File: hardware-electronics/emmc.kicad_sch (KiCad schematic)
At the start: 42 parts, among them J7 TC2030-IDC-NL, U2 EMMC16G-MW28-01E10, U4 24AA04T-I_OT, U8 USB2244-AEZG-06, Y2 ECS-240-10-47-CKM-TR

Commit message: [#26] Correct MPN GRM155R61H105KE05D
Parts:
- C11, C12, C14, C21, C7, C9: Author Your Name -> Lukasz Nowarkiewicz; MPN GRM155R61H105KE92D -> GRM155R61H105KE05D
- C17: Author Your Name -> Lukasz Nowarkiewicz; MPN GRM155R61H105KE92D -> GRM155R61H105KE05D; now left out of the parts list
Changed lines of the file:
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@@
 			)
 		)
-		(property "MPN" "GRM155R61H105KE92D"
+		(property "MPN" "GRM155R61H105KE05D"
 			(at 237.49 83.82 0)
 			(effects
@@
 			)
 		)
-		(property "Author" "Your Name"
+		(property "Author" "Lukasz Nowarkiewicz"
 			(at 245.11 83.82 0)
 			(effects
@@
 		(unit 1)
 		(exclude_from_sim no)
-		(in_bom yes)
+		(in_bom no)
 		(on_board yes)
 		(dnp no)
@@
 			)
 		)
-		(property "MPN" "GRM155R61H105KE92D"
+		(property "MPN" "GRM155R61H105KE05D"
 			(at 220.98 91.44 0)
 			(effects
@@
 			)
 		)
-		(property "Author" "Your Name"
+		(property "Author" "Lukasz Nowarkiewicz"
 			(at 228.6 91.44 0)
 			(effects
@@
 			)
 		)
-		(property "MPN" "GRM155R61H105KE92D"
+		(property "MPN" "GRM155R61H105KE05D"
 			(at 278.13 80.01 0)
 			(effects
@@
 			)
 		)
-		(property "Author" "Your Name"
+		(property "Author" "Lukasz Nowarkiewicz"
 			(at 285.75 80.01 0)
 			(effects
@@
 			)
 		)
-		(property "MPN" "GRM155R61H105KE92D"
+		(property "MPN" "GRM155R61H105KE05D"
 			(at 34.29 66.04 0)
 			(effects
@@
 			)
 		)
-		(property "Author" "Your Name"
+		(property "Author" "Lukasz Nowarkiewicz"
 			(at 41.91 66.04 0)
 			(effects
@@
 			)
 		)
-		(property "MPN" "GRM155R61H105KE92D"
+		(property "MPN" "GRM155R61H105KE05D"
 			(at 255.27 83.82 0)
 			(effects
@@
 			)
 		)
-		(property "Author" "Your Name"
+		(property "Author" "Lukasz Nowarkiewicz"
 			(at 262.89 83.82 0)
 			(effects
@@
 			)
 		)
-		(property "MPN" "GRM155R61H105KE92D"
+		(property "MPN" "GRM155R61H105KE05D"
 			(at 95.25 156.21 0)
 			(effects
@@
 			)
 		)
-		(property "Author" "Your Name"
+		(property "Author" "Lukasz Nowarkiewicz"
 			(at 102.87 156.21 0)
 			(effects
@@
 			)
 		)
-		(property "MPN" "GRM155R61H105KE92D"
+		(property "MPN" "GRM155R61H105KE05D"
 			(at 294.64 73.66 0)
 			(effects
@@
 			)
 		)
-		(property "Author" "Your Name"
+		(property "Author" "Lukasz Nowarkiewicz"
 			(at 302.26 73.66 0)
 			(effects

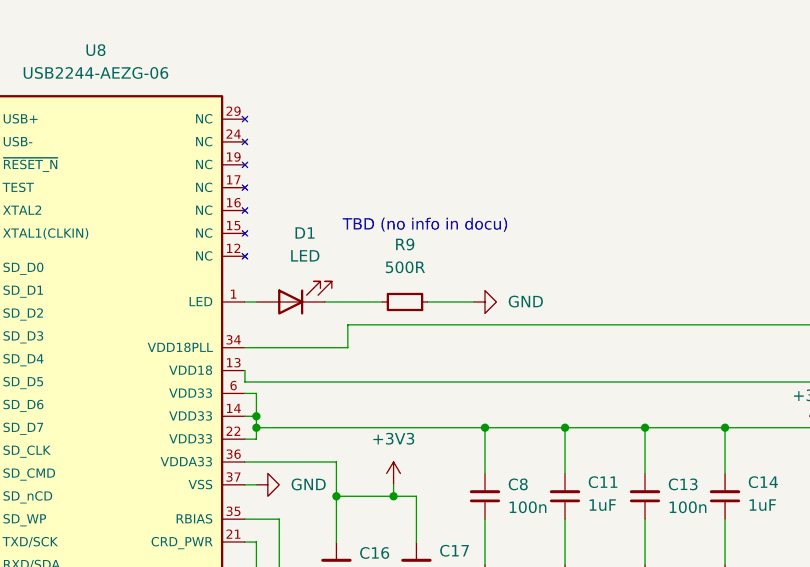
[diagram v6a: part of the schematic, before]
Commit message: [#26] Replace 500ohm to 510ohm  MPN CRCW0402510RJNED
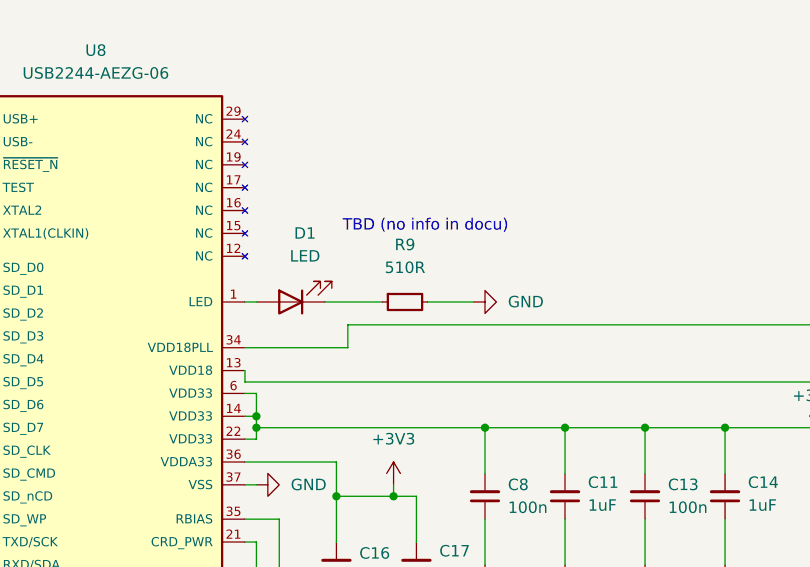
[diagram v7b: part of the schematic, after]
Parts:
- removed R9: R_500R_0402, M2SmartHomeFootprints:R_0402, symbol M2SmartHomeSymbols:R_500R_0402
- added R9: R_510R_0402, M2SmartHomeFootprints:R_0402, symbol M2SmartHomeSymbols:R_510R_0402
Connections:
- net GND: now also R9.2
- net at D1.1 (K): now also R9.1
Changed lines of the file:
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@@
+	)
+	(symbol
+		(lib_id "M2SmartHomeSymbols:R_510R_0402")
+		(at 199.39 80.01 0)
+		(unit 1)
+		(exclude_from_sim no)
+		(in_bom yes)
+		(on_board yes)
+		(dnp no)
+		(fields_autoplaced yes)
+		(property "Reference" "R9"
+			(at 201.93 73.66 0)
+			(effects
+				(font
+					(size 1.27 1.27)
+					(thickness 0.15)
+				)
+			)
+		)
+		(property "Value" "R_510R_0402"
+			(at 219.71 92.71 0)
+			(effects
+				(font
+					(size 1.27 1.27)
+					(thickness 0.15)
+				)
+				(justify left bottom)
+				(hide yes)
+			)
+		)
+		(property "Footprint" "M2SmartHomeFootprints:R_0402"
+			(at 219.71 95.25 0)
+			(effects
+				(font
+					(size 1.27 1.27)
+					(thickness 0.15)
+				)
+				(justify left bottom)
+				(hide yes)
+			)
+		)
+		(property "Datasheet" "https://www.vishay.com/docs/20035/crcw0402.pdf"
+			(at 219.71 97.79 0)
+			(effects
+				(font
+					(size 1.27 1.27)
+					(thickness 0.15)
+				)
+				(justify left bottom)
+				(hide yes)
+			)
+		)
+		(property "Description" "SMD Thick Film Resistor, 510 Ω, ±1%, 1/16 W, 0402 [1005 Metric], CRCW Series"
+			(at 199.39 80.01 0)
+			(effects
+				(font
+					(size 1.27 1.27)
+				)
+				(hide yes)
+			)
+		)
+		(property "MPN" "CRCW0402510RJNED"
+			(at 219.71 100.33 0)
+			(effects
+				(font
+					(size 1.27 1.27)
+					(thickness 0.15)
+				)
+				(justify left bottom)
+				(hide yes)
+			)
+		)
+		(property "Manufacturer" "Vishay"
+			(at 219.71 102.87 0)
+			(effects
+				(font
+					(size 1.27 1.27)
+					(thickness 0.15)
+				)
+				(justify left bottom)
+				(hide yes)
+			)
+		)
+		(property "License" "Apache-2.0"
+			(at 219.71 105.41 0)
+			(effects
+				(font
+					(size 1.27 1.27)
+					(thickness 0.15)
+				)
+				(justify left bottom)
+				(hide yes)
+			)
+		)
+		(property "Author" "Lukasz Nowarkiewicz"
+			(at 219.71 107.95 0)
+			(effects
+				(font
+					(size 1.27 1.27)
+					(thickness 0.15)
+				)
+				(justify left bottom)
+				(hide yes)
+			)
+		)
+		(property "Val" "510R"
+			(at 201.93 76.2 0)
+			(effects
+				(font
+					(size 1.27 1.27)
+					(thickness 0.15)
+				)
+			)
+		)
+		(property "Tolerance" "1%"
+			(at 219.71 90.17 0)
+			(effects
+				(font
+					(size 1.27 1.27)
+				)
+				(justify left bottom)
+				(hide yes)
+			)
+		)
+		(property "Power" "1/16 W"
+			(at 219.71 93.71 0)
+			(effects
+				(font
+					(size 1.27 1.27)
+				)
+				(justify left bottom)
+				(hide yes)
+			)
+		)
+		(pin "2"
+		)
+		(pin "1"
+		)
+		(instances
+			(project "M2SmartHome"
+				(path "/da663dec-9e91-4003-a791-431d460ad63c/d6ad415e-1295-4f8b-8193-bff1569600a2"
+					(reference "R9")
+					(unit 1)
+				)
+			)
+		)
 	)
 	(symbol
@@
 					(unit 1)
 				)
-			)
-		)
-	)
-	(symbol
-		(lib_id "M2SmartHomeSymbols:R_500R_0402")
-		(at 204.47 80.01 180)
-		(unit 1)
-		(exclude_from_sim no)
-		(in_bom yes)
-		(on_board yes)
-		(dnp no)
-		(fields_autoplaced yes)
-		(property "Reference" "R9"
-			(at 201.93 73.66 0)
-			(effects
-				(font
-					(size 1.27 1.27)
-					(thickness 0.15)
-				)
-			)
-		)
-		(property "Value" "R_500R_0402"
-			(at 184.15 67.31 0)
-			(effects
-				(font
-					(size 1.27 1.27)
-					(thickness 0.15)
-				)
-				(justify left bottom)
-				(hide yes)
-			)
-		)
-		(property "Footprint" "M2SmartHomeFootprints:R_0402"
-			(at 184.15 64.77 0)
-			(effects
-				(font
-					(size 1.27 1.27)
-					(thickness 0.15)
-				)
-				(justify left bottom)
-				(hide yes)
-			)
-		)
-		(property "Datasheet" "https://www.vishay.com/docs/20035/crcw0402.pdf"
-			(at 184.15 62.23 0)
-			(effects
-				(font
-					(size 1.27 1.27)
-					(thickness 0.15)
-				)
-				(justify left bottom)
-				(hide yes)
-			)
-		)
-		(property "Description" "SMD Thick Film Resistor, 500 Ω, ±1%, 1/16 W, 0402 [1005 Metric], CRCW Series"
-			(at 204.47 80.01 0)
-			(effects
-				(font
-					(size 1.27 1.27)
-				)
-				(hide yes)
-			)
-		)
-		(property "MPN" "CRCW0402500RFKED"
-			(at 184.15 59.69 0)
-			(effects
-				(font
-					(size 1.27 1.27)
-					(thickness 0.15)
-				)
-				(justify left bottom)
-				(hide yes)
-			)
-		)
-		(property "Manufacturer" "Vishay"
-			(at 184.15 57.15 0)
-			(effects
-				(font
-					(size 1.27 1.27)
-					(thickness 0.15)
-				)
-				(justify left bottom)
-				(hide yes)
-			)
-		)
-		(property "License" "Apache-2.0"
-			(at 184.15 54.61 0)
-			(effects
-				(font
-					(size 1.27 1.27)
-					(thickness 0.15)
-				)
-				(justify left bottom)
-				(hide yes)
-			)
-		)
-		(property "Author" "Your Name"
-			(at 184.15 52.07 0)
-			(effects
-				(font
-					(size 1.27 1.27)
-					(thickness 0.15)
-				)
-				(justify left bottom)
-				(hide yes)
-			)
-		)
-		(property "Val" "500R"
-			(at 201.93 76.2 0)
-			(effects
-				(font
-					(size 1.27 1.27)
-					(thickness 0.15)
-				)
-			)
-		)
-		(property "Tolerance" "1%"
-			(at 184.15 69.85 0)
-			(effects
-				(font
-					(size 1.27 1.27)
-				)
-				(justify left bottom)
-				(hide yes)
-			)
-		)
-		(property "Power" "1/16 W"
-			(at 184.15 66.31 0)
-			(effects
-				(font
-					(size 1.27 1.27)
-				)
-				(justify left bottom)
-				(hide yes)
-			)
-		)
-		(pin "2"
-		)
-		(pin "1"
-		)
-		(instances
-			(project "M2SmartHome"
-				(path "/da663dec-9e91-4003-a791-431d460ad63c/d6ad415e-1295-4f8b-8193-bff1569600a2"
-					(reference "R9")
-					(unit 1)
-				)

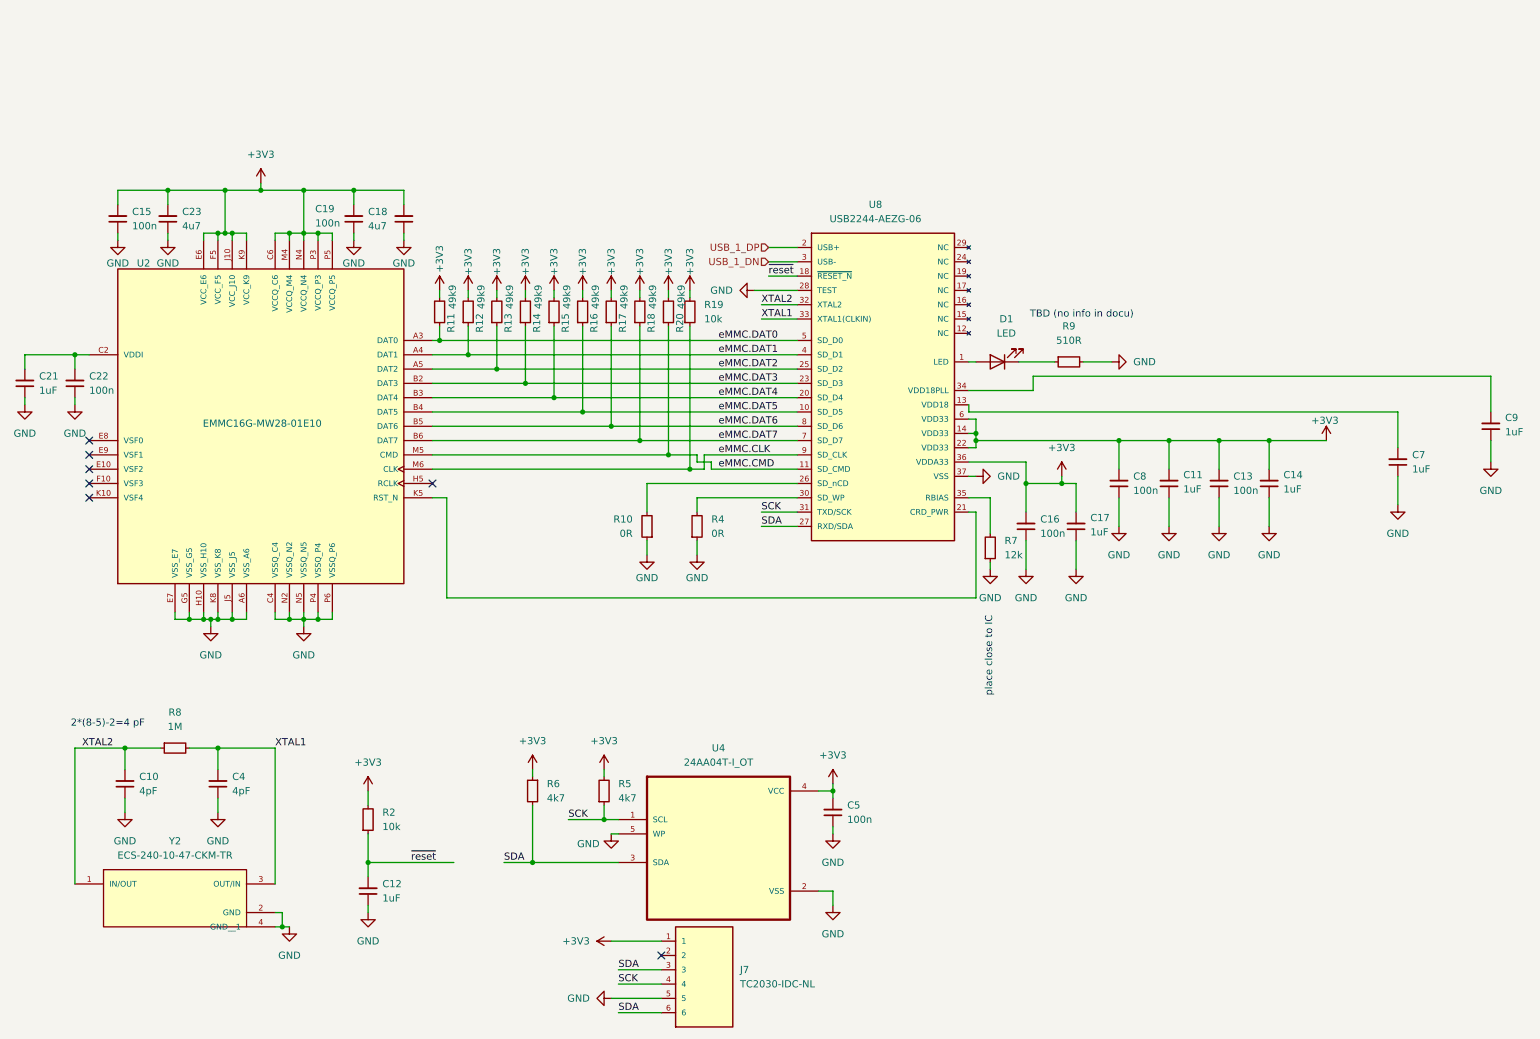
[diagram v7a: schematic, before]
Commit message: [#26] Add I2C EEPROM for emmc and usd ICP
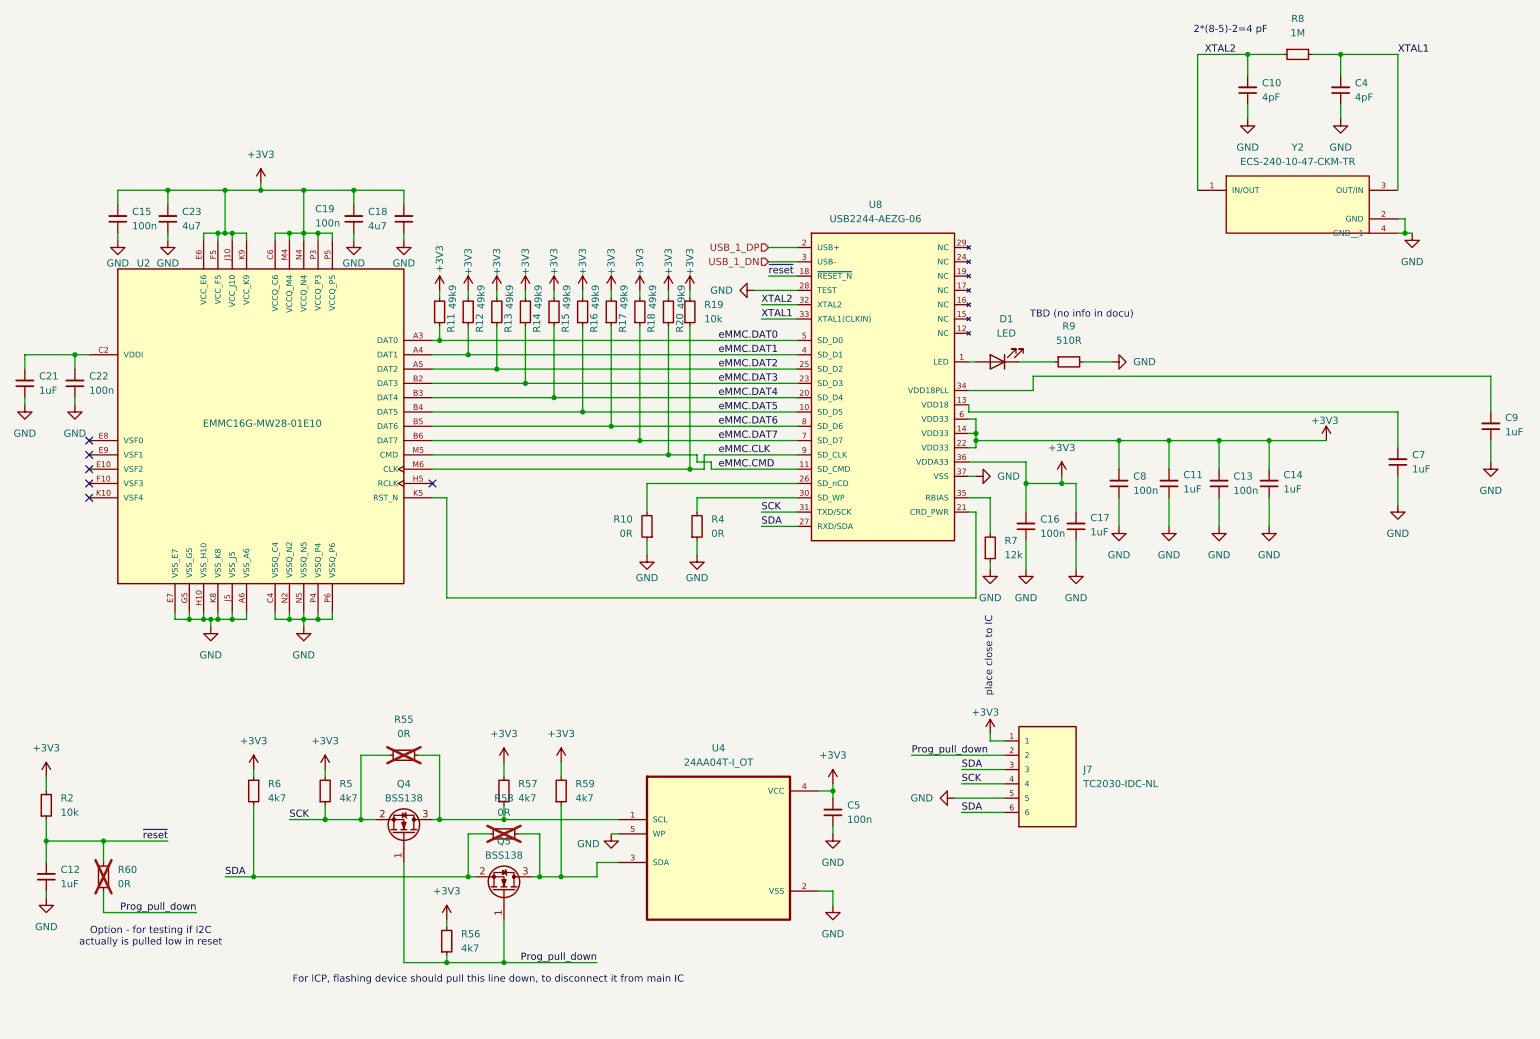
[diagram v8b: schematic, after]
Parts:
- added Q4, Q5: BSS138, Package_TO_SOT_SMD:SOT-23, symbol Transistor_FET:BSS138
- added R55, R58, R60: R_0_0402, M2SmartHomeFootprints:R_0402, symbol M2SmartHomeSymbols:R_0_0402
- added R56, R57, R59: R_4k7_0402, M2SmartHomeFootprints:R_0402, symbol M2SmartHomeSymbols:R_4k7_0402
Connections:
- net +3V3: now also R56.2, R57.2, R59.2
- net SCK: now also Q4.2 (S), R55.2; no longer U4.1 (SCL)
- net SDA: now also Q5.2 (S), R58.2; no longer U4.3 (SDA)
- net ~{reset}: now also R60.1
- net Prog_pull_down: now reaches J7.2
- net Prog_pull_down: now also Q4.1 (G), Q5.1 (G), R56.1, R60.2
- new net: Q5.3 (D), R58.1, R59.1, U4.3 (SDA)
- new net: Q4.3 (D), R55.1, R57.1, U4.1 (SCL)
- no-connect marks 7 -> 6
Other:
- note added: "For ICP, flashing device should pull this line down, to disconnect it from main IC"
- note added: "Option - for testing if I2C actually is pulled low in reset"
- moved on the sheet: C10, C12, C4, J7, R2, R5, R6, R8, Y2
